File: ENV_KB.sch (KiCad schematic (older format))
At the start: 180 parts, among them J1 TYPE-C-31-M-12

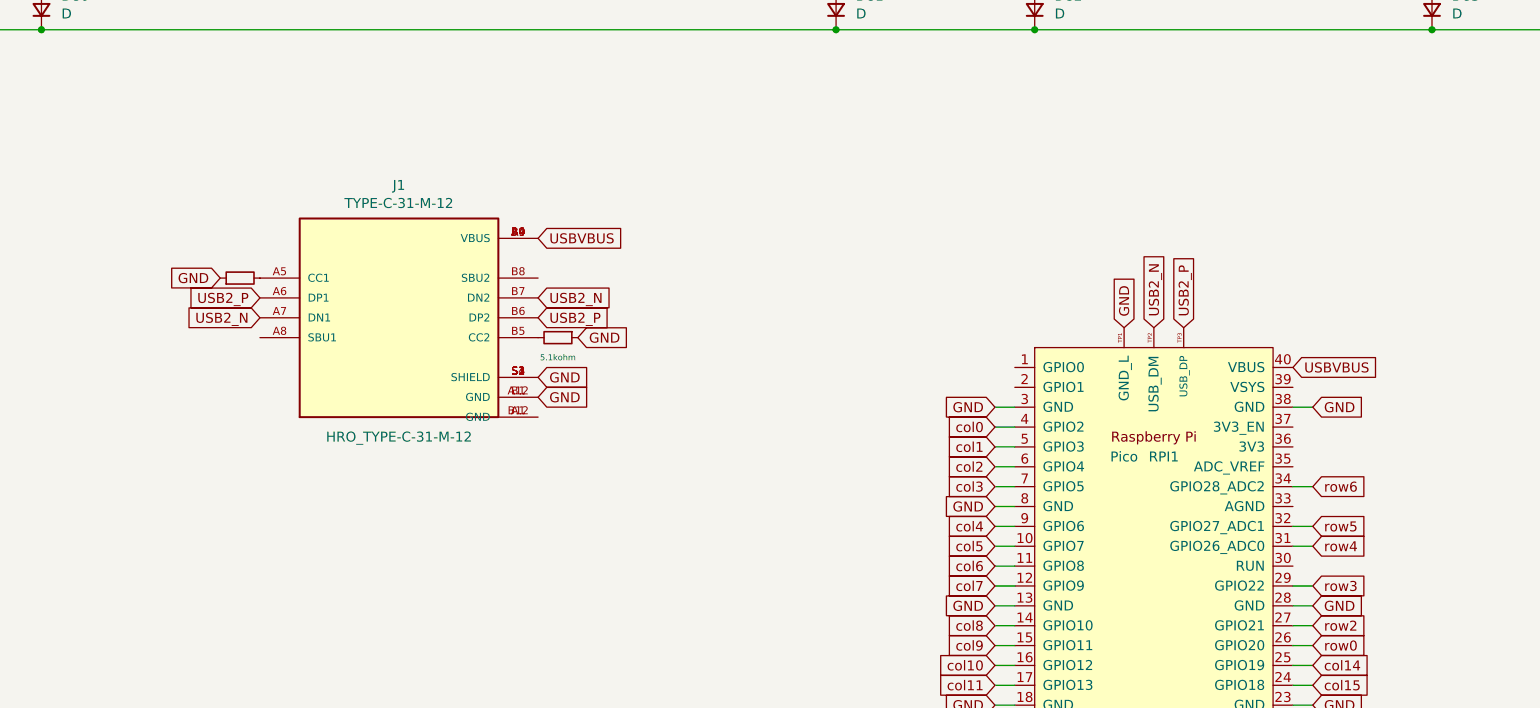
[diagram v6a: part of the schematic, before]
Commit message: Upgrade to #d4e7e293a4b4e92c8b19c42b1b3e7286d16a446a
Adjustments for Rev.B

added a place for the I2C header and traces + a USB power LED and a few small tweaks
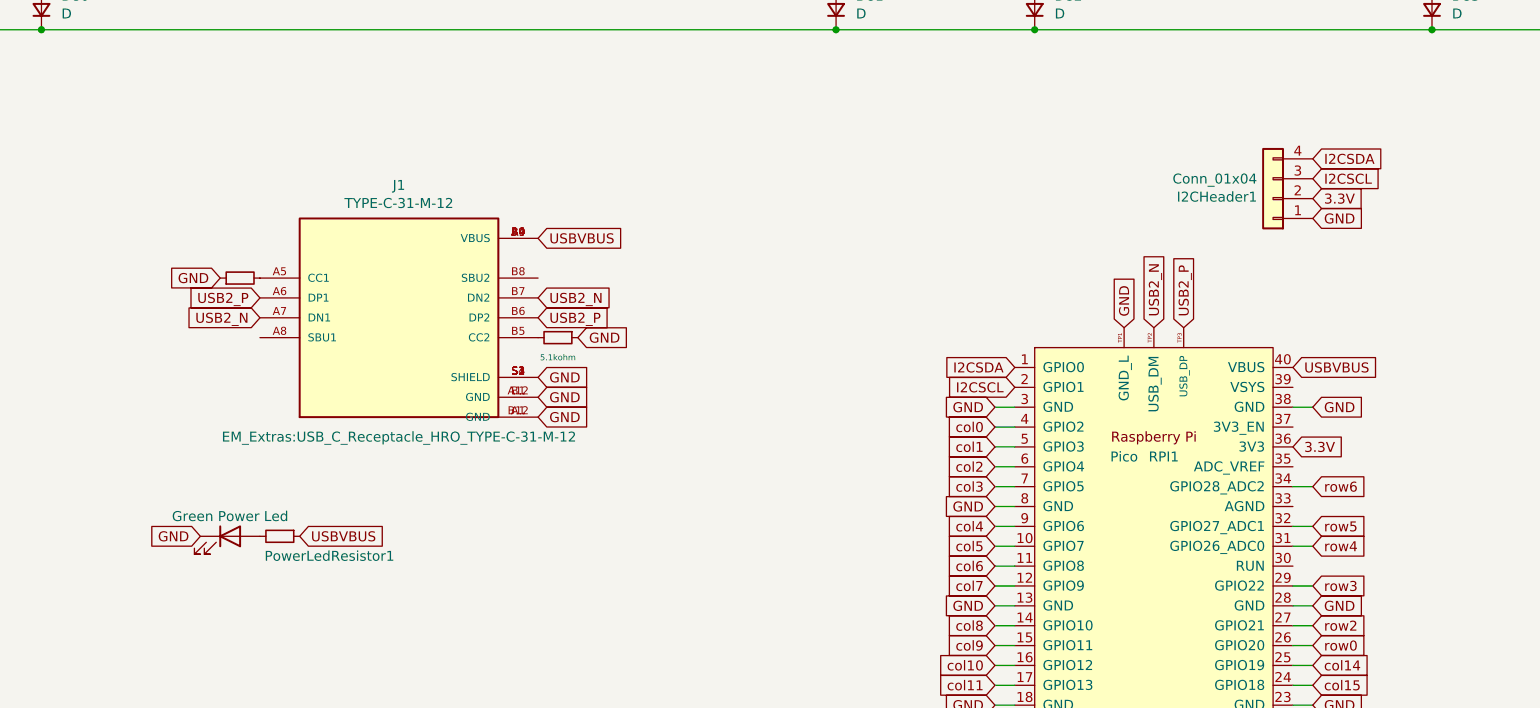
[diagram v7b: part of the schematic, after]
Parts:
- added I2CHeader1: Conn_01x04, Connector_PinSocket_2.54mm:PinSocket_1x04_P2.54mm_Vertical, symbol Connector_Generic:Conn_01x04
- added PowerLED1: Green Power Led, LED_SMD:LED_0805_2012Metric, symbol Device:LED
- added PowerLedResistor1: 1K Resistor, Resistor_SMD:R_0805_2012Metric, symbol Device:R_Small
- J1: footprint HRO_TYPE-C-31-M-12 -> EM_Extras:USB_C_Receptacle_HRO_TYPE-C-31-M-12
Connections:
- net GND: now also J1.A1 (GND), J1.B12 (GND), I2CHeader1.1 (Pin_1), PowerLED1.1 (K)
- net USBVBUS: now also PowerLedResistor1.1
- net I2CSDA: now reaches RPI1.1 (GPIO0)
- net I2CSDA: now also I2CHeader1.4 (Pin_4)
- net I2CSCL: now reaches RPI1.2 (GPIO1)
- net I2CSCL: now also I2CHeader1.3 (Pin_3)
- net 3.3V: now reaches RPI1.36 (3V3)
- net 3.3V: now also I2CHeader1.2 (Pin_2)
- new net: PowerLED1.2 (A), PowerLedResistor1.2
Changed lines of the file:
@@
 Text GLabel 9850 9250 2    50   Input ~ 0
 GND
+Text GLabel 9850 8750 2    50   Input ~ 0
+USB2_N
+Text GLabel 8450 8750 0    50   Input ~ 0
+USB2_P
+$Comp
+L Device:LED PowerLED1
+U 1 1 6043F14D
+P 8300 9950
+F 0 "PowerLED1" H 8293 10167 50  0001 C CNN
+F 1 "Green Power Led" H 8300 10050 50  0000 C CNN
+F 2 "LED_SMD:LED_0805_2012Metric" H 8300 9950 50  0001 C CNN
+F 3 "~" H 8300 9950 50  0001 C CNN
+	1    8300 9950
+	1    0    0    -1
+$EndComp
+Text GLabel 8150 9950 0    50   Input ~ 0
+GND
+Text GLabel 8650 9950 2    50   Input ~ 0
+USBVBUS
+$Comp
+L Device:R_Small PowerLedResistor1
+U 1 1 604A80B1
+P 8550 9950
+F 0 "PowerLedResistor1" V 8650 10200 50  0000 C CNN
+F 1 "1K Resistor" V 8700 10000 50  0001 C CNN
+F 2 "Resistor_SMD:R_0805_2012Metric" H 8550 9950 50  0001 C CNN
+F 3 "~" H 8550 9950 50  0001 C CNN
+	1    8550 9950
+	0    1    1    0
+$EndComp
 $Comp
 L Type-C-Lib:TYPE-C-31-M-12 J1
@@
 F 0 "J1" H 9150 9517 50  0000 C CNN
 F 1 "TYPE-C-31-M-12" H 9150 9426 50  0000 C CNN
-F 2 "HRO_TYPE-C-31-M-12" H 9150 8250 50  0000 C CNN
+F 2 "EM_Extras:USB_C_Receptacle_HRO_TYPE-C-31-M-12" H 9150 8250 50  0000 C CNN
 F 3 "~" H 9300 8850 50  0001 C CNN
 F 4 "HRO Electronics" H 9150 8850 50  0001 C CNN "MANUFACTURER"
@@
 	1    0    0    -1
 $EndComp
-Text GLabel 9850 8750 2    50   Input ~ 0
-USB2_N
-Text GLabel 8450 8750 0    50   Input ~ 0
-USB2_P
+Text GLabel 9850 9350 2    50   Input ~ 0
+GND
+$Comp
+L Connector_Generic:Conn_01x04 I2CHeader1
+U 1 1 605CD72C
+P 13550 8250
+F 0 "I2CHeader1" H 13630 8242 50  0000 L CNN
+F 1 "Conn_01x04" H 13630 8151 50  0000 L CNN
+F 2 "Connector_PinSocket_2.54mm:PinSocket_1x04_P2.54mm_Vertical" H 13550 8250 50  0001 C CNN
+F 3 "~" H 13550 8250 50  0001 C CNN
+	1    13550 8250
+	-1   0    0    1
+$EndComp
+Text GLabel 12250 9100 0    50   Input ~ 0
+I2CSDA
+Text GLabel 12250 9200 0    50   Input ~ 0
+I2CSCL
+Text GLabel 13650 9500 2    50   Input ~ 0
+3.3V
+Text GLabel 13750 8050 2    50   Input ~ 0
+I2CSDA
+Text GLabel 13750 8150 2    50   Input ~ 0
+I2CSCL
+Text GLabel 13750 8350 2    50   Input ~ 0
+GND
+Text GLabel 13750 8250 2    50   Input ~ 0
+3.3V
 $EndSCHEMATC

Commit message: Corrections, Part Numbers, Cleanups, etc
I removed a couple of un-needed libraries finally and corrected a bunch of stuff.

also added LSCS part numbers in the schematic

probably some other stuff I forgot
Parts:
- J1: LSCS Part (none) -> C165948
- PowerLED1: footprint LED_SMD:LED_0805_2012Metric -> LED_SMD:LED_0805_2012Metric_Castellated; LSCS Part (none) -> C2297
- PowerLedResistor1: LSCS Part (none) -> C17513
- RESISTOR1, RESISTOR2: LSCS Part (none) -> C25905
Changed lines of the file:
@@
 F 2 "Resistor_SMD:R_0402_1005Metric" H 9950 8950 50  0001 C CNN
 F 3 "~" H 9950 8950 50  0001 C CNN
+F 4 "C25905" V 9950 8950 50  0001 C CNN "LSCS Part"
 	1    9950 8950
 	0    1    1    0
@@
 F 2 "Resistor_SMD:R_0402_1005Metric" H 8350 8650 50  0001 C CNN
 F 3 "~" H 8350 8650 50  0001 C CNN
+F 4 "C25905" V 8350 8650 50  0001 C CNN "LSCS Part"
 	1    8350 8650
 	0    -1   -1   0
@@
 F 0 "PowerLED1" H 8293 10167 50  0001 C CNN
 F 1 "Green Power Led" H 8300 10050 50  0000 C CNN
-F 2 "LED_SMD:LED_0805_2012Metric" H 8300 9950 50  0001 C CNN
+F 2 "LED_SMD:LED_0805_2012Metric_Castellated" H 8300 9950 50  0001 C CNN
 F 3 "~" H 8300 9950 50  0001 C CNN
+F 4 "C2297" H 8300 9950 50  0001 C CNN "LSCS Part"
 	1    8300 9950
 	1    0    0    -1
@@
 F 2 "Resistor_SMD:R_0805_2012Metric" H 8550 9950 50  0001 C CNN
 F 3 "~" H 8550 9950 50  0001 C CNN
+F 4 "C17513" V 8550 9950 50  0001 C CNN "LSCS Part"
 	1    8550 9950
 	0    1    1    0
@@
 F 6 "A" H 9150 8850 50  0001 C CNN "PARTREV"
 F 7 "Manufacturer Recommendations" H 9150 8850 50  0001 C CNN "STANDARD"
+F 8 "C165948" H 9150 8850 50  0001 C CNN "LSCS Part"
 	1    9150 8850
 	1    0    0    -1
